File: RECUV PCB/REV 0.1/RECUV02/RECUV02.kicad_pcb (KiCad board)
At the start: 2 copper layers, 140 x 105.5 mm, 77 parts, among them P1 VEXT, P2 VOLTAGE, P3 CURRENT, Q1 MMBT2222ALT1, Q2 MMBT2222ALT1, U1 ESP32-S3-WROOM-1, U2 CH340C, U3 A1117-3.3, U4 RESET, U5 BOOT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

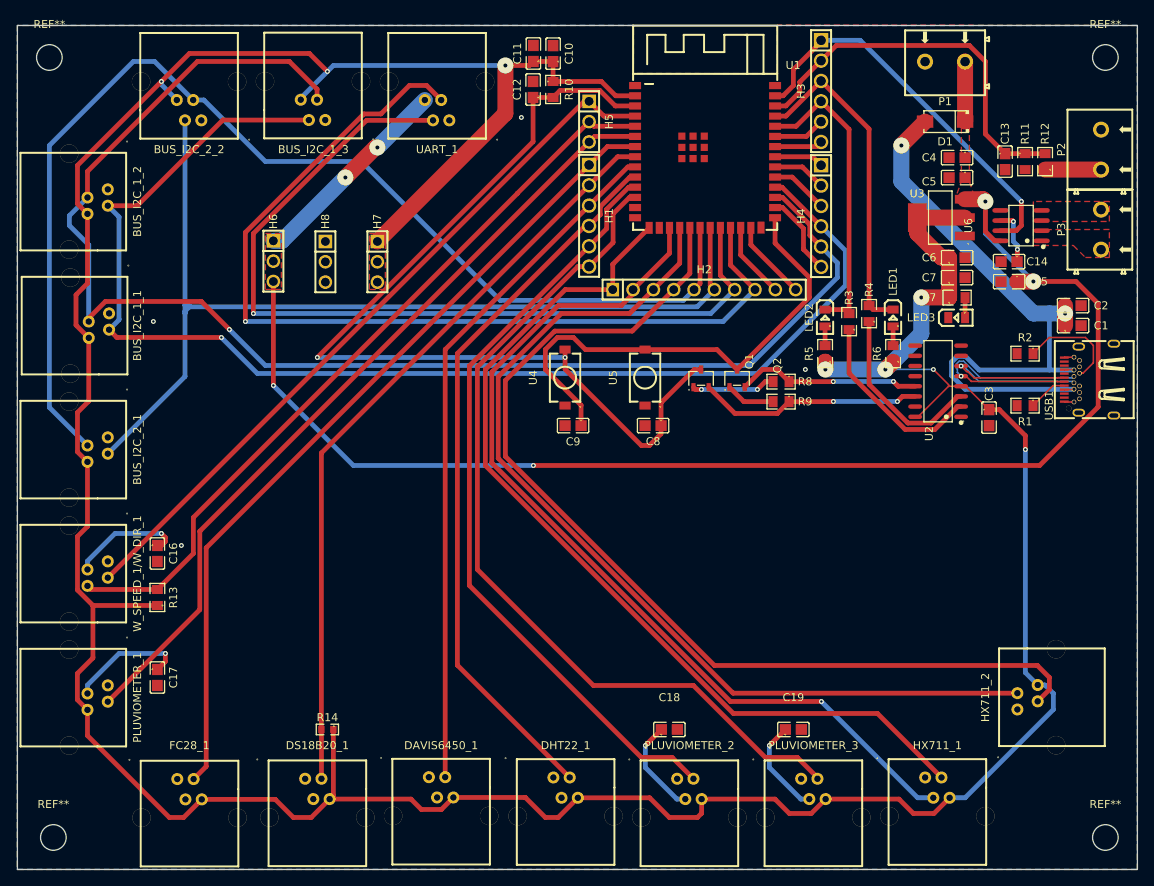
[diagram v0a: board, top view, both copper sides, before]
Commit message: Corrected PCB Form
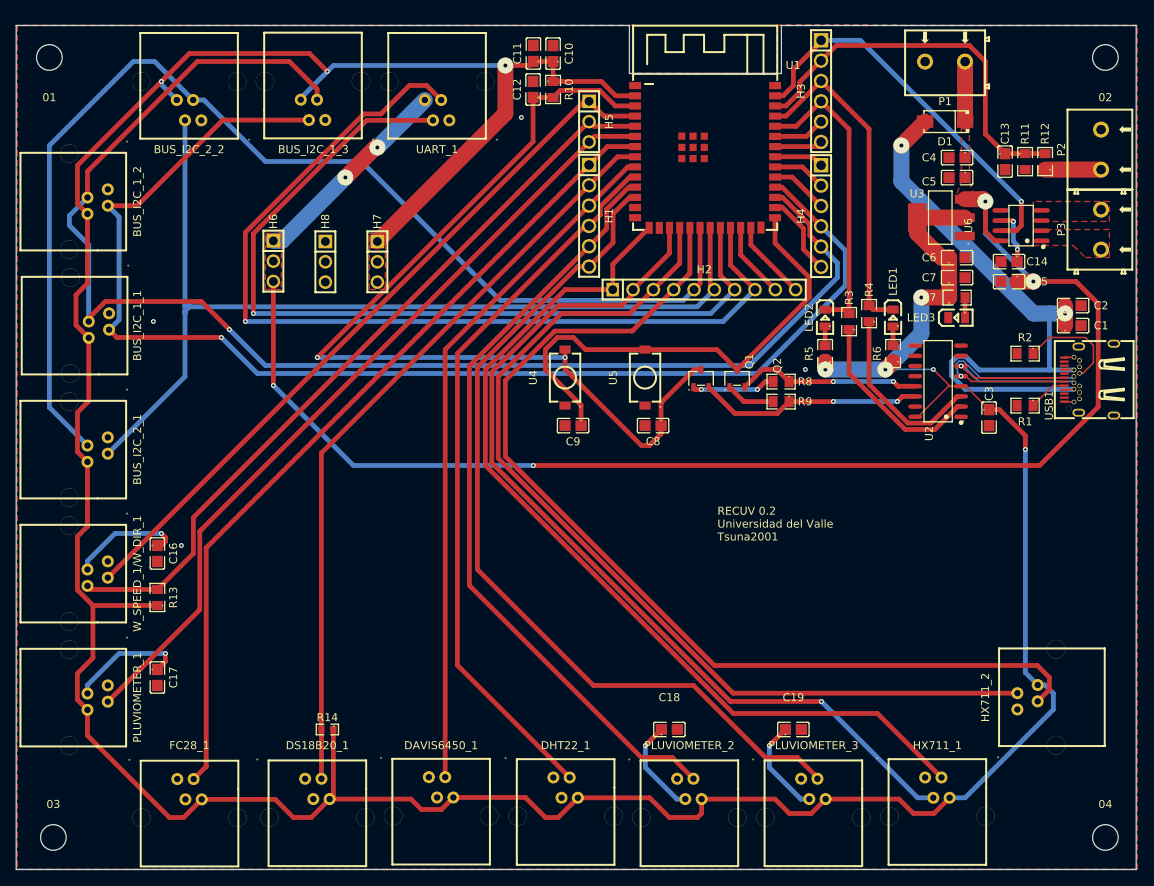
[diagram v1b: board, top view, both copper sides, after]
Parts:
- renumbered REF** to 01, REF** to 02, REF** to 03, REF** to 04
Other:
- outline, holes or cut-outs redrawn
- board text added: "RECUV 0.2 Universidad del Valle Tsuna2001"
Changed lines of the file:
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@@
 		(descr "Mounting Hole 3.2mm, M3, no annular, generated by kicad-footprint-generator mountinghole.py")
 		(tags "mountinghole M3")
-		(property "Reference" "REF**"
-			(at 0 -4.15 0)
+		(property "Reference" "02"
+			(at 0 5 0)
 			(layer "F.SilkS")
 			(effects
@@
 		(descr "Mounting Hole 3.2mm, M3, no annular, generated by kicad-footprint-generator mountinghole.py")
 		(tags "mountinghole M3")
-		(property "Reference" "REF**"
-			(at 0 -4.15 0)
+		(property "Reference" "01"
+			(at 0 5 0)
 			(layer "F.SilkS")
 			(effects
@@
 		(descr "Mounting Hole 3.2mm, M3, no annular, generated by kicad-footprint-generator mountinghole.py")
 		(tags "mountinghole M3")
-		(property "Reference" "REF**"
+		(property "Reference" "04"
 			(at 0 -4.15 0)
 			(layer "F.SilkS")
@@
 		(descr "Mounting Hole 3.2mm, M3, no annular, generated by kicad-footprint-generator mountinghole.py")
 		(tags "mountinghole M3")
-		(property "Reference" "REF**"
+		(property "Reference" "03"
 			(at 0 -4.15 0)
 			(layer "F.SilkS")
@@
 		)
 	)
-	(gr_rect
-		(start 33 23)
-		(end 173 128.5)
+	(gr_poly
+		(pts
+			(xy 32.852348 23) (xy 109.5 23) (xy 109.500178 29.000545) (xy 128.5 29) (xy 128.5 23) (xy 172.852348 23)
+			(xy 172.852348 128.5) (xy 32.852348 128.5)
+		)
 		(stroke
 			(width 0.05)
-			(type default)
+			(type solid)
 		)
 		(fill no)
 		(layer "Edge.Cuts")
 	)
+	(gr_text "RECUV 0.2\nUniversidad del Valle\nTsuna2001"
+		(at 120.5 87.5 0)
+		(layer "F.SilkS")
+		(effects
+			(font
+				(size 1 1)
+				(thickness 0.1)
+			)
+			(justify left bottom)
+		)
+	)
 	(segment
